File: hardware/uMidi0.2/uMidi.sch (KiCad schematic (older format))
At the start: 36 parts, among them CON1 USB-MINI-B, IC1 6N138, IC2 ATXMEGA128A4U-M, P1 MIDI In, P2 MIDI Thru, P3 MIDI T/O, P4 MIDI Out, P5 5..12 V, P6 PDI, U1 74LS14, U2 LT1129CST-3.3

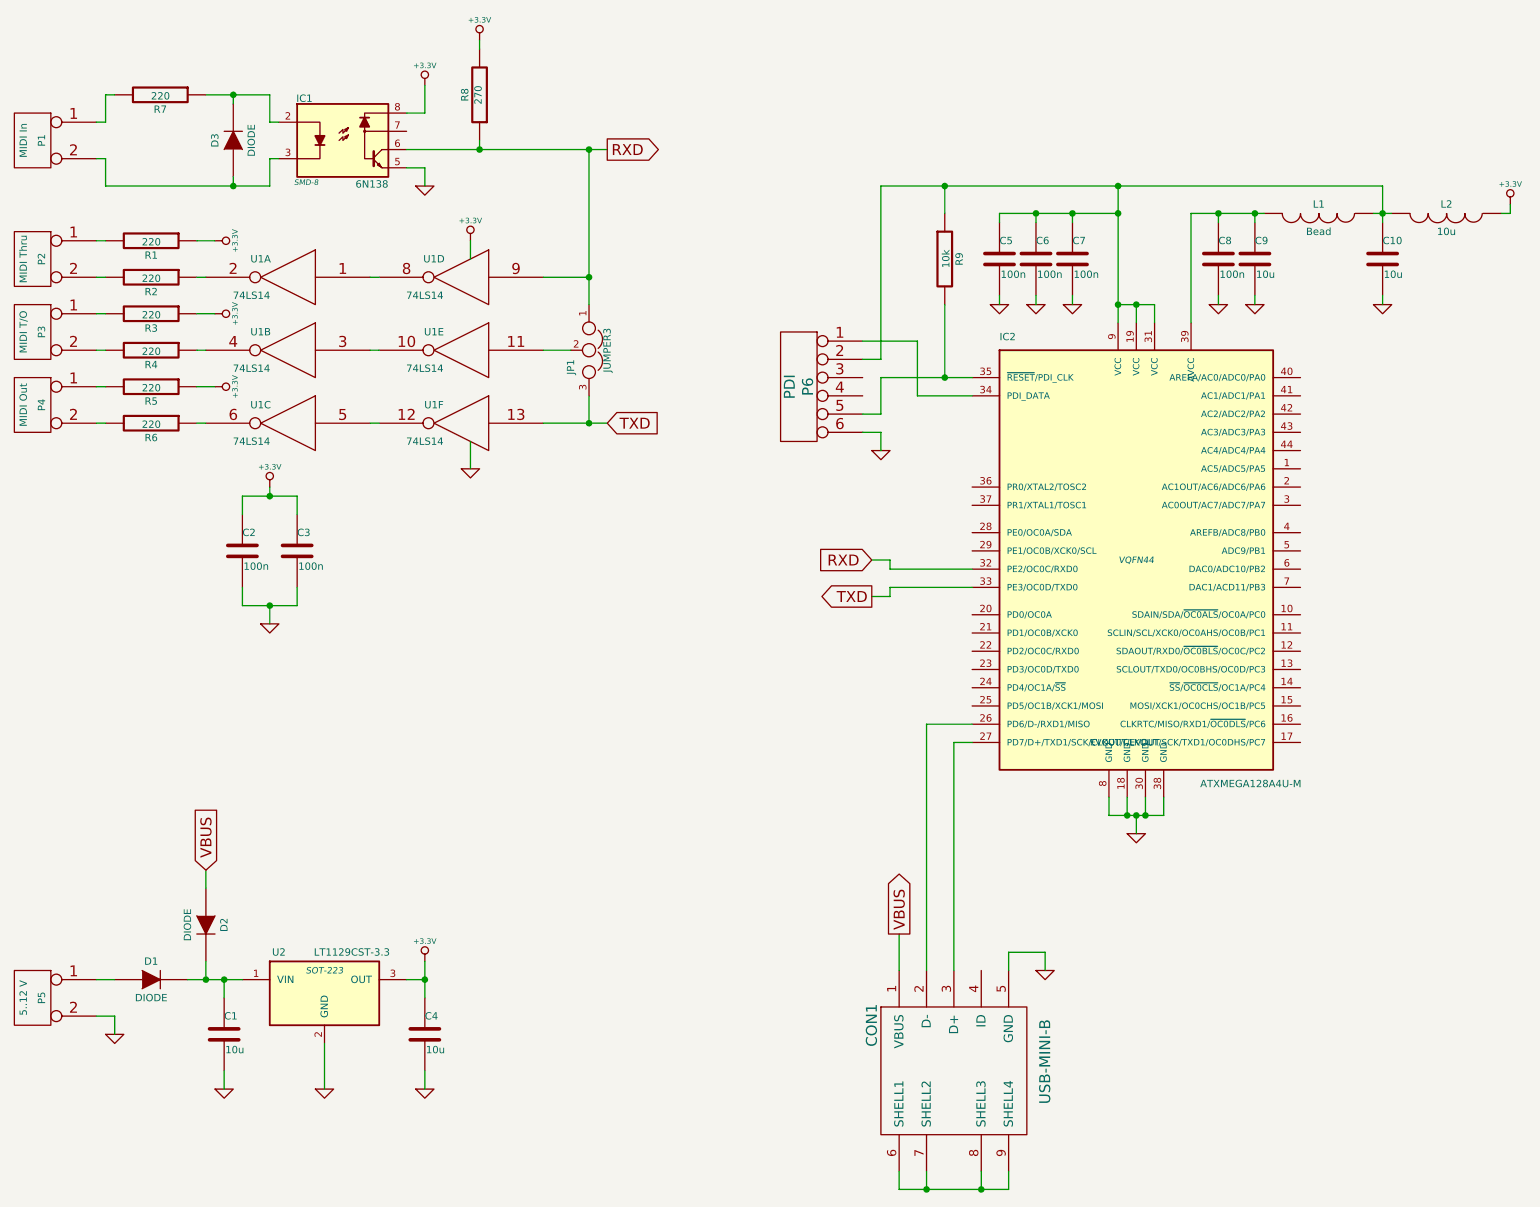
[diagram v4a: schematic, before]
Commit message: Add gpio connectors
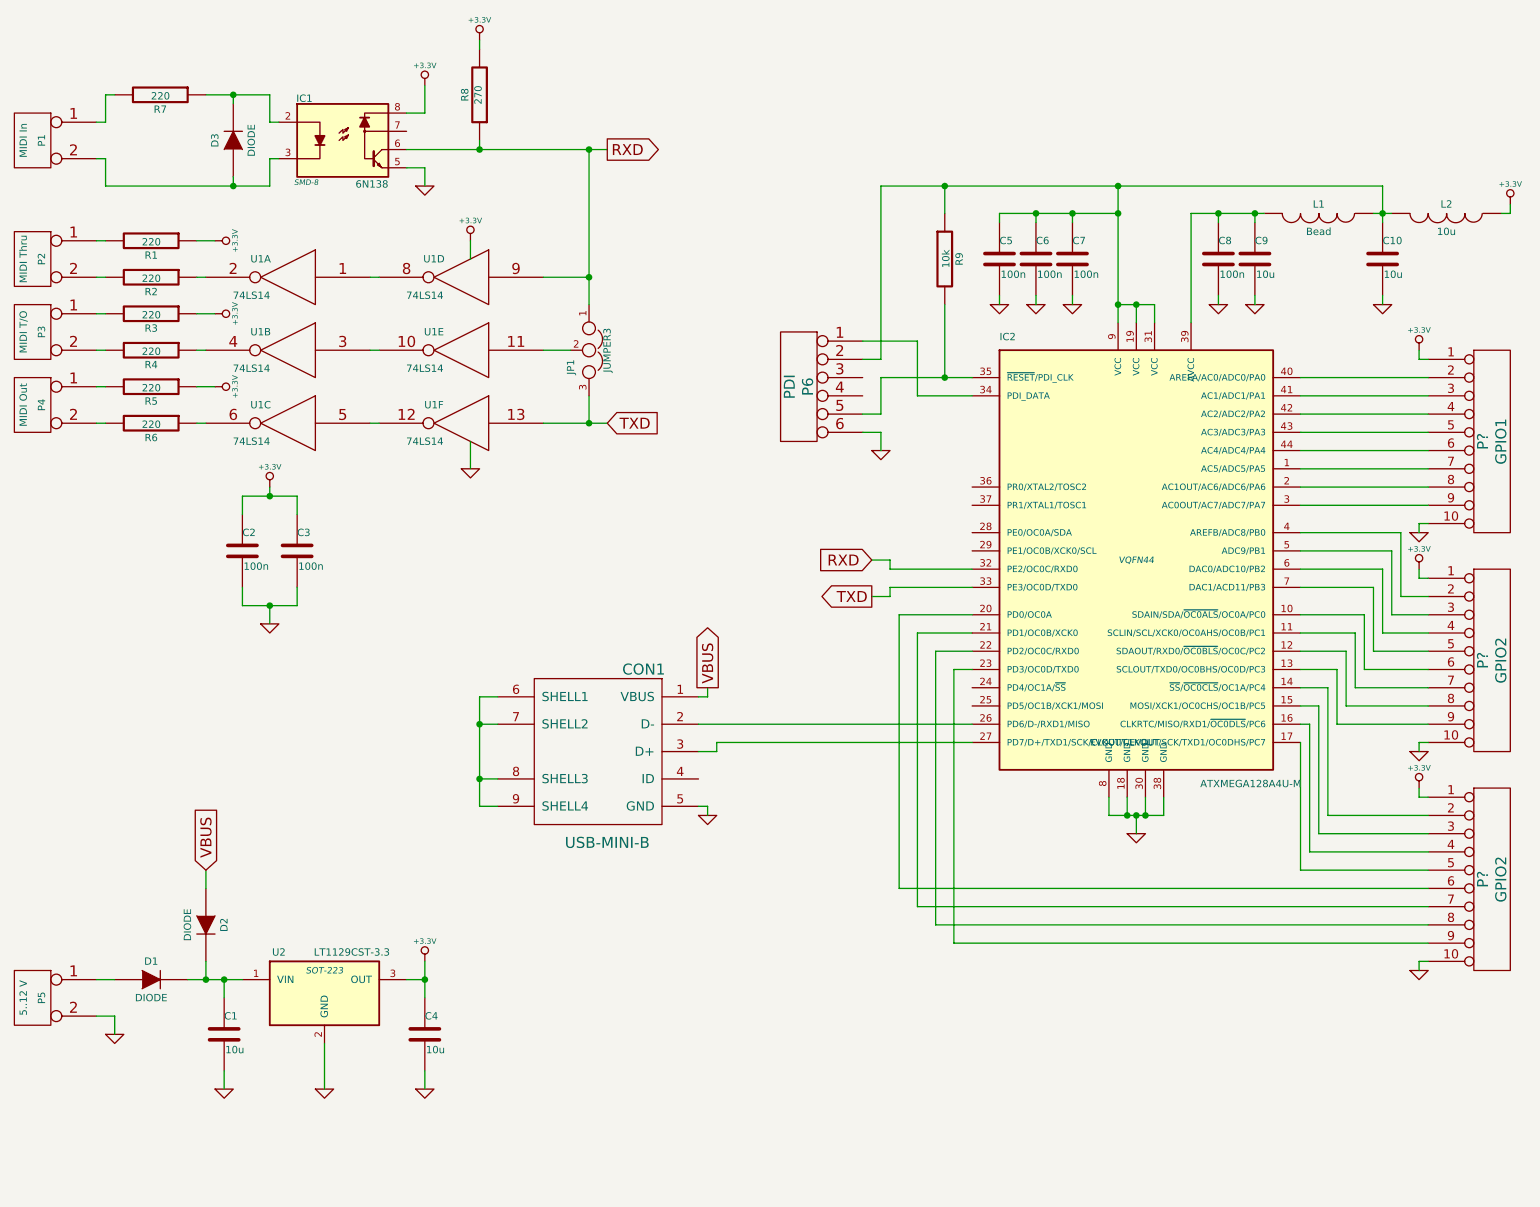
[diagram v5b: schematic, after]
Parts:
- added P?: GPIO1, symbol CONN_10
- added P? (x2): GPIO2, symbol CONN_10
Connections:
- net +3.3V: now also P?.1 (P1), P?.1 (P1), P?.1 (P1)
- net GND: now also P?.10 (P10), P?.10 (P10), P?.10 (P10)
- net at IC2.1 (AC5/ADC5/PA5): now also P?.7 (P7)
- net at IC2.10 (SDAIN/SDA/~OC0ALS~/OC0A/PC0): now also P?.6 (P6)
- net at IC2.11 (SCLIN/SCL/XCK0/OC0AHS/OC0B/PC1): now also P?.7 (P7)
- net at IC2.12 (SDAOUT/RXD0/~OC0BLS~/OC0C/PC2): now also P?.8 (P8)
- net at IC2.13 (SCLOUT/TXD0/OC0BHS/OC0D/PC3): now also P?.9 (P9)
- net at IC2.14 (~SS~/~OC0CLS~/OC1A/PC4): now also P?.2 (P2)
- net at IC2.15 (MOSI/XCK1/OC0CHS/OC1B/PC5): now also P?.3 (P3)
- net at IC2.16 (CLKRTC/MISO/RXD1/~OC0DLS~/PC6): now also P?.4 (P4)
- net at IC2.17 (EVOUT/CLKOUT/SCK/TXD1/OC0DHS/PC7): now also P?.5 (P5)
- net at IC2.2 (AC1OUT/AC6/ADC6/PA6): now also P?.8 (P8)
- net at IC2.20 (PD0/OC0A): now also P?.6 (P6)
- net at IC2.21 (PD1/OC0B/XCK0): now also P?.7 (P7)
- net at IC2.22 (PD2/OC0C/RXD0): now also P?.8 (P8)
- net at IC2.23 (PD3/OC0D/TXD0): now also P?.9 (P9)
- net at IC2.3 (AC0OUT/AC7/ADC7/PA7): now also P?.9 (P9)
- net at IC2.4 (AREFB/ADC8/PB0): now also P?.2 (P2)
- net at IC2.40 (AREFA/AC0/ADC0/PA0): now also P?.2 (P2)
- net at IC2.41 (AC1/ADC1/PA1): now also P?.3 (P3)
- net at IC2.42 (AC2/ADC2/PA2): now also P?.4 (P4)
- net at IC2.43 (AC3/ADC3/PA3): now also P?.5 (P5)
- net at IC2.44 (AC4/ADC4/PA4): now also P?.6 (P6)
- net at IC2.5 (ADC9/PB1): now also P?.3 (P3)
- net at IC2.6 (DAC0/ADC10/PB2): now also P?.4 (P4)
- net at IC2.7 (DAC1/ACD11/PB3): now also P?.5 (P5)
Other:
- moved on the sheet: CON1

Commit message: Add crystal
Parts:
- added C5, C6: 15p, symbol C
- added X1: 32MHz, symbol QUARTZCMS4
- gave numbers to parts that had none: 3
- renumbered C8 to C10, C9 to C11, C10 to C12, C5 to C7, C6 to C8, C7 to C9
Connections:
- net GND: now also C5.1, C6.1
- net at IC2.36 (PR0/XTAL2/TOSC2): now also C5.2, X1.1
- net at IC2.37 (PR1/XTAL1/TOSC1): now also C6.2, X1.3
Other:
- moved on the sheet: P6
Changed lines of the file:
@@
 $EndComp
 $Comp
-L GND #PWR21
+L GND #PWR23
 U 1 1 53C6C394
 P 7200 5250
-F 0 "#PWR21" H 7200 5250 30  0001 C CNN
+F 0 "#PWR23" H 7200 5250 30  0001 C CNN
 F 1 "GND" H 7200 5180 30  0001 C CNN
 F 2 "" H 7200 5250 60  0000 C CNN
@@
 $EndComp
 $Comp
-L +3.3V #PWR25
+L +3.3V #PWR33
 U 1 1 53C6C3CA
 P 9250 1800
-F 0 "#PWR25" H 9250 1760 30  0001 C CNN
+F 0 "#PWR33" H 9250 1760 30  0001 C CNN
 F 1 "+3.3V" H 9250 1910 30  0000 C CNN
 F 2 "" H 9250 1800 60  0000 C CNN
@@
 L CONN_6 P6
 U 1 1 53C6CF68
-P 5350 2800
-F 0 "P6" V 5300 2800 60  0000 C CNN
-F 1 "PDI" V 5400 2800 60  0000 C CNN
-F 2 "" H 5350 2800 60  0000 C CNN
-F 3 "" H 5350 2800 60  0000 C CNN
-	1    5350 2800
+P 5350 2600
+F 0 "P6" V 5300 2600 60  0000 C CNN
+F 1 "PDI" V 5400 2600 60  0000 C CNN
+F 2 "" H 5350 2600 60  0000 C CNN
+F 3 "" H 5350 2600 60  0000 C CNN
+	1    5350 2600
 	-1   0    0    -1
 $EndComp
 $Comp
-L GND #PWR16
+L GND #PWR19
 U 1 1 53C6D292
-P 5800 3150
-F 0 "#PWR16" H 5800 3150 30  0001 C CNN
-F 1 "GND" H 5800 3080 30  0001 C CNN
-F 2 "" H 5800 3150 60  0000 C CNN
-F 3 "" H 5800 3150 60  0000 C CNN
-	1    5800 3150
+P 5750 2900
+F 0 "#PWR19" H 5750 2900 30  0001 C CNN
+F 1 "GND" H 5750 2830 30  0001 C CNN
+F 2 "" H 5750 2900 60  0000 C CNN
+F 3 "" H 5750 2900 60  0000 C CNN
+	1    5750 2900
 	1    0    0    -1
 $EndComp
@@
 	7300 2350 7300 2450
 Wire Wire Line
-	5800 2750 6300 2750
-Wire Wire Line
-	6150 2350 6150 2750
-Wire Wire Line
-	5700 2550 6000 2550
-Wire Wire Line
-	6000 2550 6000 2850
+	6150 2750 6150 2350
+Wire Wire Line
+	5700 2350 6000 2350
+Wire Wire Line
+	6000 2350 6000 2850
 Wire Wire Line
 	6000 2850 6300 2850
 Wire Wire Line
-	5800 2650 5700 2650
-Wire Wire Line
-	5800 3150 5800 3050
-Wire Wire Line
-	5800 3050 5700 3050
-Wire Wire Line
-	5800 2750 5800 2950
-Wire Wire Line
-	5800 2950 5700 2950
+	5800 2450 5700 2450
+Wire Wire Line
+	5700 2750 6300 2750
 Connection ~ 6150 2750
 Wire Wire Line
@@
 Connection ~ 3600 4650
 $Comp
-L GND #PWR19
+L GND #PWR16
 U 1 1 53C6DAEC
 P 4850 5150
-F 0 "#PWR19" H 4850 5150 30  0001 C CNN
+F 0 "#PWR16" H 4850 5150 30  0001 C CNN
 F 1 "GND" H 4850 5080 30  0001 C CNN
 F 2 "" H 4850 5150 60  0000 C CNN
@@
 Text GLabel 4300 1500 2    60   Output ~ 0
 RXD
-Text GLabel 5750 3750 0    60   Input ~ 0
+Text GLabel 6200 3800 0    60   Input ~ 0
 RXD
 Text GLabel 4300 3000 2    60   Input ~ 0
 TXD
-Text GLabel 5750 3950 0    60   Output ~ 0
+Text GLabel 6200 3950 0    60   Output ~ 0
 TXD
-Wire Wire Line
-	6300 3800 5850 3800
-Wire Wire Line
-	5850 3800 5850 3750
-Wire Wire Line
-	5850 3750 5750 3750
-Wire Wire Line
-	5750 3950 5850 3950
-Wire Wire Line
-	5850 3950 5850 3900
-Wire Wire Line
-	5850 3900 6300 3900
-$Comp
-L C C5
+$Comp
+L C C7
 U 1 1 53CA9538
 P 6450 2100
-F 0 "C5" H 6450 2200 40  0000 L CNN
+F 0 "C7" H 6450 2200 40  0000 L CNN
 F 1 "100n" H 6456 2015 40  0000 L CNN
 F 2 "" H 6488 1950 30  0000 C CNN
@@
 $EndComp
 $Comp
-L C C6
+L C C8
 U 1 1 53CA95D0
 P 6650 2100
-F 0 "C6" H 6650 2200 40  0000 L CNN
+F 0 "C8" H 6650 2200 40  0000 L CNN
 F 1 "100n" H 6656 2015 40  0000 L CNN
 F 2 "" H 6688 1950 30  0000 C CNN
@@
 $EndComp
 $Comp
-L C C7
+L C C9
 U 1 1 53CA95DB
 P 6850 2100
-F 0 "C7" H 6850 2200 40  0000 L CNN
+F 0 "C9" H 6850 2200 40  0000 L CNN
 F 1 "100n" H 6856 2015 40  0000 L CNN
 F 2 "" H 6888 1950 30  0000 C CNN
@@
 $EndComp
 $Comp
-L C C10
+L C C12
 U 1 1 53CA95EC
 P 8550 2100
-F 0 "C10" H 8550 2200 40  0000 L CNN
+F 0 "C12" H 8550 2200 40  0000 L CNN
 F 1 "10u" H 8556 2015 40  0000 L CNN
 F 2 "" H 8588 1950 30  0000 C CNN
@@
 	6450 1900 6450 1850
 $Comp
-L GND #PWR17
+L GND #PWR20
 U 1 1 53CA9815
 P 6450 2350
-F 0 "#PWR17" H 6450 2350 30  0001 C CNN
+F 0 "#PWR20" H 6450 2350 30  0001 C CNN
 F 1 "GND" H 6450 2280 30  0001 C CNN
 F 2 "" H 6450 2350 60  0000 C CNN
@@
 $EndComp
 $Comp
-L GND #PWR18
+L GND #PWR21
 U 1 1 53CA9834
 P 6650 2350
-F 0 "#PWR18" H 6650 2350 30  0001 C CNN
+F 0 "#PWR21" H 6650 2350 30  0001 C CNN
 F 1 "GND" H 6650 2280 30  0001 C CNN
 F 2 "" H 6650 2350 60  0000 C CNN
@@
 $EndComp
 $Comp
-L GND #PWR20
+L GND #PWR22
 U 1 1 53CA983F
 P 6850 2350
-F 0 "#PWR20" H 6850 2350 30  0001 C CNN
+F 0 "#PWR22" H 6850 2350 30  0001 C CNN
 F 1 "GND" H 6850 2280 30  0001 C CNN
 F 2 "" H 6850 2350 60  0000 C CNN
@@
 $EndComp
 $Comp
-L GND #PWR24
+L GND #PWR26
 U 1 1 53CA984A
 P 8550 2350
-F 0 "#PWR24" H 8550 2350 30  0001 C CNN
+F 0 "#PWR26" H 8550 2350 30  0001 C CNN
 F 1 "GND" H 8550 2280 30  0001 C CNN
 F 2 "" H 8550 2350 60  0000 C CNN
@@
 $EndComp
 $Comp
-L C C9
+L C C11
 U 1 1 53CA9C01
 P 7850 2100
-F 0 "C9" H 7850 2200 40  0000 L CNN
+F 0 "C11" H 7850 2200 40  0000 L CNN
 F 1 "10u" H 7856 2015 40  0000 L CNN
 F 2 "" H 7888 1950 30  0000 C CNN
@@
 $EndComp
 $Comp
-L C C8
+L C C10
 U 1 1 53CA9C0C
 P 7650 2100
-F 0 "C8" H 7650 2200 40  0000 L CNN
+F 0 "C10" H 7650 2200 40  0000 L CNN
 F 1 "100n" H 7656 2015 40  0000 L CNN
 F 2 "" H 7688 1950 30  0000 C CNN
@@
 Connection ~ 7650 1850
 $Comp
-L GND #PWR22
+L GND #PWR24
 U 1 1 53CA9EF0
 P 7650 2350
-F 0 "#PWR22" H 7650 2350 30  0001 C CNN
+F 0 "#PWR24" H 7650 2350 30  0001 C CNN
 F 1 "GND" H 7650 2280 30  0001 C CNN
 F 2 "" H 7650 2350 60  0000 C CNN
@@
 $EndComp
 $Comp
-L GND #PWR23
+L GND #PWR25
 U 1 1 53CA9EFB
 P 7850 2350
-F 0 "#PWR23" H 7850 2350 30  0001 C CNN
+F 0 "#PWR25" H 7850 2350 30  0001 C CNN
 F 1 "GND" H 7850 2280 30  0001 C CNN
 F 2 "" H 7850 2350 60  0000 C CNN
@@
 Wire Wire Line
 	6150 1700 6150 1850
-Wire Wire Line
-	5800 2650 5800 1700
 Connection ~ 6150 1700
 Connection ~ 7100 1700
@@
 Connection ~ 2450 3400
 $Comp
-L CONN_10 P?
+L CONN_10 P7
 U 1 1 53CAB25D
 P 9150 3100
-F 0 "P?" V 9100 3100 60  0000 C CNN
+F 0 "P7" V 9100 3100 60  0000 C CNN
 F 1 "GPIO1" V 9200 3100 60  0000 C CNN
 F 2 "" H 9150 3100 60  0000 C CNN
@@
 	8800 3450 8100 3450
 $Comp
-L GND #PWR?
+L GND #PWR28
 U 1 1 53CAB87E
 P 8750 3600
-F 0 "#PWR?" H 8750 3600 30  0001 C CNN
+F 0 "#PWR28" H 8750 3600 30  0001 C CNN
 F 1 "GND" H 8750 3530 30  0001 C CNN
 F 2 "" H 8750 3600 60  0000 C CNN
@@
 	8750 3550 8800 3550
 $Comp
-L +3.3V #PWR?
+L +3.3V #PWR27
 U 1 1 53CAB929
 P 8750 2600
-F 0 "#PWR?" H 8750 2560 30  0001 C CNN
+F 0 "#PWR27" H 8750 2560 30  0001 C CNN
 F 1 "+3.3V" H 8750 2710 30  0000 C CNN
 F 2 "" H 8750 2600 60  0000 C CNN
@@
 	8750 2650 8800 2650
 $Comp
-L CONN_10 P?
+L CONN_10 P8
 U 1 1 53CAB9DB
 P 9150 4300
-F 0 "P?" V 9100 4300 60  0000 C CNN
+F 0 "P8" V 9100 4300 60  0000 C CNN
 F 1 "GPIO2" V 9200 4300 60  0000 C CNN
 F 2 "" H 9150 4300 60  0000 C CNN
@@
 $EndComp
 $Comp
-L +3.3V #PWR?
+L +3.3V #PWR29
 U 1 1 53CAB9E6
 P 8750 3800
-F 0 "#PWR?" H 8750 3760 30  0001 C CNN
+F 0 "#PWR29" H 8750 3760 30  0001 C CNN
 F 1 "+3.3V" H 8750 3910 30  0000 C CNN
 F 2 "" H 8750 3800 60  0000 C CNN
@@
 	8300 4650 8800 4650
 $Comp
-L GND #PWR?
+L GND #PWR30
 U 1 1 53CAC1E9
 P 8750 4800
-F 0 "#PWR?" H 8750 4800 30  0001 C CNN
+F 0 "#PWR30" H 8750 4800 30  0001 C CNN
 F 1 "GND" H 8750 4730 30  0001 C CNN
 F 2 "" H 8750 4800 60  0000 C CNN
@@
 	8750 4750 8800 4750
 $Comp
-L CONN_10 P?
+L CONN_10 P9
 U 1 1 53CAC3EE
 P 9150 5500
-F 0 "P?" V 9100 5500 60  0000 C CNN
+F 0 "P9" V 9100 5500 60  0000 C CNN
 F 1 "GPIO2" V 9200 5500 60  0000 C CNN
 F 2 "" H 9150 5500 60  0000 C CNN
@@
 	5900 4050 6300 4050
 $Comp
-L GND #PWR?
+L GND #PWR32
 U 1 1 53CAD159
 P 8750 6000
-F 0 "#PWR?" H 8750 6000 30  0001 C CNN
+F 0 "#PWR32" H 8750 6000 30  0001 C CNN
 F 1 "GND" H 8750 5930 30  0001 C CNN
 F 2 "" H 8750 6000 60  0000 C CNN
@@
 $EndComp
 $Comp
-L +3.3V #PWR?
+L +3.3V #PWR31
 U 1 1 53CAD164
 P 8750 5000
-F 0 "#PWR?" H 8750 4960 30  0001 C CNN
+F 0 "#PWR31" H 8750 4960 30  0001 C CNN
 F 1 "+3.3V" H 8750 5110 30  0000 C CNN
 F 2 "" H 8750 5000 60  0000 C CNN
@@
 Wire Wire Line
 	8750 5950 8800 5950
+$Comp
+L QUARTZCMS4 X1
+U 1 1 53CAD6C6
+P 6050 3400
+F 0 "X1" H 6050 3550 60  0000 C CNN
+F 1 "32MHz" H 6050 3250 60  0000 C CNN
+F 2 "" H 6050 3400 60  0000 C CNN
+F 3 "" H 6050 3400 60  0000 C CNN
+	1    6050 3400
+	0    1    1    0
+$EndComp
+Wire Wire Line
+	6200 3800 6300 3800
+Wire Wire Line
+	6200 3950 6250 3950
+Wire Wire Line
+	6250 3950 6250 3900
+Wire Wire Line
+	6250 3900 6300 3900
+Wire Wire Line
+	6000 3700 6200 3700
+Wire Wire Line
+	6200 3700 6200 3500
+Wire Wire Line
+	6200 3500 6300 3500
+Wire Wire Line
+	6300 3500 6300 3450
+Wire Wire Line
+	6300 3350 6300 3300
+Wire Wire Line
+	6300 3300 6200 3300
+Wire Wire Line
+	6200 3300 6200 3100
+Wire Wire Line
+	6200 3100 6000 3100
+$Comp
+L C C6
+U 1 1 53CADAB7
+P 5800 3700
+F 0 "C6" H 5800 3800 40  0000 L CNN
+F 1 "15p" H 5806 3615 40  0000 L CNN
+F 2 "" H 5838 3550 30  0000 C CNN
+F 3 "" H 5800 3700 60  0000 C CNN
+	1    5800 3700
+	0    -1   -1   0
+$EndComp
+Wire Wire Line
+	5800 2450 5800 1700
+$Comp
+L C C5
+U 1 1 53CADE7D
+P 5800 3100
+F 0 "C5" H 5800 3200 40  0000 L CNN
+F 1 "15p" H 5806 3015 40  0000 L CNN
+F 2 "" H 5838 2950 30  0000 C CNN
+F 3 "" H 5800 3100 60  0000 C CNN
+	1    5800 3100
+	0    -1   -1   0
+$EndComp
+Wire Wire Line
+	5700 2850 5750 2850
+Wire Wire Line
+	5750 2850 5750 2900
+Connection ~ 6050 3100
+Connection ~ 6050 3700
+$Comp
+L GND #PWR18
+U 1 1 53CAE196
+P 5550 3700
+F 0 "#PWR18" H 5550 3700 30  0001 C CNN
+F 1 "GND" H 5550 3630 30  0001 C CNN
+F 2 "" H 5550 3700 60  0000 C CNN
+F 3 "" H 5550 3700 60  0000 C CNN
+	1    5550 3700
+	0    1    1    0
+$EndComp
+$Comp
+L GND #PWR17
+U 1 1 53CAE1A6
+P 5550 3100
+F 0 "#PWR17" H 5550 3100 30  0001 C CNN
+F 1 "GND" H 5550 3030 30  0001 C CNN
+F 2 "" H 5550 3100 60  0000 C CNN
+F 3 "" H 5550 3100 60  0000 C CNN
+	1    5550 3100
+	0    1    1    0
+$EndComp
+Wire Wire Line
+	5550 3100 5600 3100
+Wire Wire Line
+	5550 3700 5600 3700
 $EndSCHEMATC
